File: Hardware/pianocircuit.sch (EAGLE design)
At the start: 180 parts

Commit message: Updated Schematic
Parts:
- removed C10, C13, C14, C16, C17, C18, C19, C20, C26, C27, C28, C29, C30, C38, C39, C40, C41, C42, C50, C51, C52, C53, C54, C8, C9: (no value), LinnesLab-Passives:CAPACITOR0603
- removed C15, C25, C37, C49, C7: 100n, LinnesLab-Passives:CAPACITOR0603
- removed OP13, OP14, OP17, OP18, OP3, OP4, OP5, OP7, OP8, OP9: (no value), LinnesLab-AnalogIC:OP-DUALR
- removed R10, R19, R33, R42, R55, R73: 3.3M, LinnesLab-Passives:RESISTOR0603
- removed R11, R12, R13, R14, R20, R21, R22, R23, R34, R35, R36, R37, R56, R57, R58, R59, R74, R75, R76, R77: 10k, LinnesLab-Passives:RESISTOR0603
- removed R15, R16, R17, R18, R24, R25, R31, R32, R38, R39, R40, R41, R60, R61, R62, R63, R78, R79, R80, R81: (no value), LinnesLab-Passives:RESISTOR0603
- removed SW3, SW4, SW5, SW7, SW9: (no value), LinnesLab-Switches:SPST.KT11P4SM34LFS
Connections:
- removed net N$100: SW9.B
- removed net N$13: OP3A.+IN, R13.1, R14.2
- removed net N$14: C7.2, OP3A.-IN, OP3A.OUT, R12.1
- removed net N$15: OP3B.-IN, R11.1, R12.2
- removed net N$16: C7.1, OP3B.+IN, R10.1
- removed net N$17: OP3B.OUT, R10.2, R11.2, R15.1
- removed net N$18: C9.1, R15.2, R16.1
- removed net N$19: C10.1, R16.2, R17.1
- removed net N$20: C13.1, R17.2, R18.1
- removed net N$21: C14.1, OP4A.+IN, R18.2
- removed net N$22: OP4A.-IN, OP4A.OUT, SW3.A
- removed net N$23: SW3.B
- removed net N$24: OP5A.+IN, R22.1, R23.2
- removed net N$25: C15.2, OP5A.-IN, OP5A.OUT, R21.1
- removed net N$26: OP5B.-IN, R20.1, R21.2
- removed net N$32: C15.1, OP5B.+IN, R19.1
- removed net N$33: OP5B.OUT, R19.2, R20.2, R24.1
- removed net N$34: C17.1, R24.2, R25.1
- removed net N$35: C18.1, R25.2, R31.1
- removed net N$36: C19.1, R31.2, R32.1
- removed net N$37: C20.1, OP7A.+IN, R32.2
- removed net N$38: OP7A.-IN, OP7A.OUT, SW4.A
- removed net N$39: SW4.B
- removed net N$40: OP8A.+IN, R36.1, R37.2
- removed net N$41: C25.2, OP8A.-IN, OP8A.OUT, R35.1
- removed net N$42: OP8B.-IN, R34.1, R35.2
- removed net N$43: C25.1, OP8B.+IN, R33.1
- removed net N$44: OP8B.OUT, R33.2, R34.2, R38.1
- removed net N$45: C27.1, R38.2, R39.1
- removed net N$46: C28.1, R39.2, R40.1
- removed net N$47: C29.1, R40.2, R41.1
- removed net N$48: C30.1, OP9A.+IN, R41.2
- removed net N$49: OP9A.-IN, OP9A.OUT, SW5.A
- removed net N$50: SW5.B
- removed net N$68: OP13A.+IN, R58.1, R59.2
- removed net N$69: C37.2, OP13A.-IN, OP13A.OUT, R57.1
- removed net N$70: OP13B.-IN, R56.1, R57.2
- removed net N$71: C37.1, OP13B.+IN, R55.1
- removed net N$72: OP13B.OUT, R55.2, R56.2, R60.1
- removed net N$73: C39.1, R60.2, R61.1
- removed net N$74: C40.1, R61.2, R62.1
- removed net N$75: C41.1, R62.2, R63.1
- removed net N$76: C42.1, OP14A.+IN, R63.2
- removed net N$77: OP14A.-IN, OP14A.OUT, SW7.A
- removed net N$78: SW7.B
- removed net N$90: OP17A.+IN, R76.1, R77.2
- removed net N$91: C49.2, OP17A.-IN, OP17A.OUT, R75.1
- removed net N$92: OP17B.-IN, R74.1, R75.2
- removed net N$93: C49.1, OP17B.+IN, R73.1
- removed net N$94: OP17B.OUT, R73.2, R74.2, R78.1
- removed net N$95: C51.1, R78.2, R79.1
- removed net N$96: C52.1, R79.2, R80.1
- removed net N$97: C53.1, R80.2, R81.1
- removed net N$98: C54.1, OP18A.+IN, R81.2
- removed net N$99: OP18A.-IN, OP18A.OUT, SW9.A
- net GND: no longer C10.2, C13.2, C14.2, C17.2, C18.2, C19.2, C20.2, C27.2, C28.2, C29.2, C30.2, C39.2, C40.2, C41.2, C42.2, C51.2, C52.2, C53.2, C54.2, C9.2, OP13P.V-, OP17P.V-, OP3P.V-, OP5P.V-, OP8P.V-, R14.1, R23.1, R37.1, R59.1, R77.1
- net N$2: no longer C16.1, C26.1, C38.1, C50.1, C8.1
- net N$60: no longer R42.1
- net N$61: no longer R42.2
- net V_BATT: no longer C16.2, C26.2, C38.2, C50.2, C8.2, OP13P.V+, OP17P.V+, OP3P.V+, OP5P.V+, OP8P.V+, R13.2, R22.2, R36.2, R58.2, R76.2
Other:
- moved on the sheet: C43, C44, C45, C46, C47, C48, OP15B, OP15P, OP16A, R64, R65, R66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

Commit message: Full Schematic
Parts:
- removed C43, C55: 100n, LinnesLab-Passives:CAPACITOR0603
- removed C44, C45, C46, C47, C48, C56, C57, C58, C59, C60: (no value), LinnesLab-Passives:CAPACITOR0603
- removed OP15, OP16, OP19, OP20: (no value), LinnesLab-AnalogIC:OP-DUALR
- removed R64, R82: 3.3M, LinnesLab-Passives:RESISTOR0603
- removed R65, R66, R67, R68, R83, R84, R85, R86: 10k, LinnesLab-Passives:RESISTOR0603
- removed R69, R70, R71, R72, R87, R88, R89, R90: (no value), LinnesLab-Passives:RESISTOR0603
- removed SW10, SW8: (no value), LinnesLab-Switches:SPST.KT11P4SM34LFS
- added C10: 330p, LinnesLab-Passives:CAPACITOR0603
- added C13: 50n, LinnesLab-Passives:CAPACITOR0603
- added C14: 250u, LinnesLab-Passives:CAPACITOR.POLARC-EEU-FM-A-220UF
- added C7, C8, C9: 33n, LinnesLab-Passives:CAPACITOR0603
- added IC1: LM386M-1, linear:LM386M-1
- added OP3: (no value), LinnesLab-AnalogIC:OP-DUALR
- added R10, R11, R12: 39k, LinnesLab-Passives:RESISTOR0603
- added R13, R14, R16: 10k, LinnesLab-Passives:RESISTOR0603
- added R15: 390k, LinnesLab-Passives:RESISTOR0603
- added R17: (no value), LinnesLab-Passives:R-TRIMM-CB10V
- added SPK1: (no value), LinnesLab-Electromechanical:SPEAKER
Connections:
- removed net N$101: OP19A.+IN, R85.1, R86.2
- removed net N$102: C55.2, OP19A.-IN, OP19A.OUT, R84.1
- removed net N$103: OP19B.-IN, R83.1, R84.2
- removed net N$104: C55.1, OP19B.+IN, R82.1
- removed net N$105: OP19B.OUT, R82.2, R83.2, R87.1
- removed net N$106: C57.1, R87.2, R88.1
- removed net N$107: C58.1, R88.2, R89.1
- removed net N$108: C59.1, R89.2, R90.1
- removed net N$109: C60.1, OP20A.+IN, R90.2
- removed net N$110: OP20A.-IN, OP20A.OUT, SW10.A
- removed net N$111: SW10.B
- removed net N$12: SW2.B
- removed net N$59: SW1.B
- removed net N$67: SW6.B
- removed net N$79: OP15A.+IN, R67.1, R68.2
- removed net N$80: C43.2, OP15A.-IN, OP15A.OUT, R66.1
- removed net N$81: OP15B.-IN, R65.1, R66.2
- removed net N$82: C43.1, OP15B.+IN, R64.1
- removed net N$83: OP15B.OUT, R64.2, R65.2, R69.1
- removed net N$84: C45.1, R69.2, R70.1
- removed net N$85: C46.1, R70.2, R71.1
- removed net N$86: C47.1, R71.2, R72.1
- removed net N$87: C48.1, OP16A.+IN, R72.2
- removed net N$88: OP16A.-IN, OP16A.OUT, SW8.A
- removed net N$89: SW8.B
- new net A3: R12.2, SW6.B
- new net C3: R10.2, SW2.B
- new net F3: R11.2, SW1.B
- new net N$14: C7.2, R10.1
- new net N$15: C10.2, C7.1, C8.1, C9.1, OP3A.+IN, R15.2
- new net N$16: C9.2, R12.1
- new net N$17: C8.2, R11.1
- new net N$20: C10.1, OP3A.OUT, R15.1, R17.E
- new net N$21: OP3A.-IN, R13.1, R14.1
- new net N$22: IC1.-IN, R17.S
- new net N$23: C13.2, R16.2
- new net N$26: C13.1, C14.+, IC1.OUT
- new net N$32: C14.-, SPK1.+
- net GND: now also IC1.+IN, IC1.GND, R14.2, R16.1, SPK1.-; no longer C45.2, C46.2, C47.2, C48.2, C57.2, C58.2, C59.2, C60.2, OP15P.V-, OP19P.V-, R68.1, R86.1
- net N$2: no longer C44.1, C56.1
- net V_BATT: now also IC1.VS, R13.2; no longer C44.2, C56.2, OP15P.V+, OP19P.V+, R67.2, R85.2

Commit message: Updated Schematic
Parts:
- removed C2, C32: (no value), LinnesLab-Passives:CAPACITOR0603
- removed R4, R45, R46, R5: 10k, LinnesLab-Passives:RESISTOR0603
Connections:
- removed net N$1: OP1A.+IN, R4.1, R5.2
- removed net N$28: C11.2, OP6A.-IN, OP6A.OUT, R28.1
- removed net N$51: OP10A.+IN, R45.1, R46.2
- removed net N$56: C31.2, OP10A.-IN, OP10A.OUT, R44.1
- net GND: no longer OP10P.V-, OP1P.V-, R46.1, R5.1
- net N$2: no longer C2.1, C32.1
- net N$3: now also C11.2, C31.2, OP6A.-IN, OP6A.OUT, R28.1, R44.1; no longer OP1A.-IN, OP1A.OUT
- net V_BATT: no longer C2.2, C32.2, OP10P.V+, OP1P.V+, R4.2, R45.2

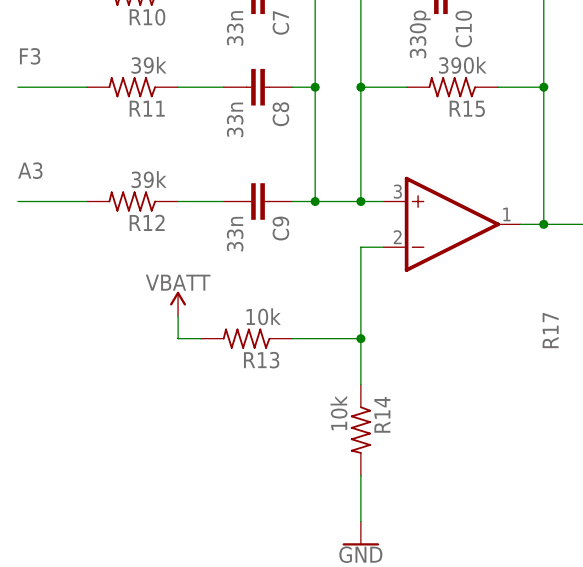
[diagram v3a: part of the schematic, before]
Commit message: Routed Board and Updated Schematic
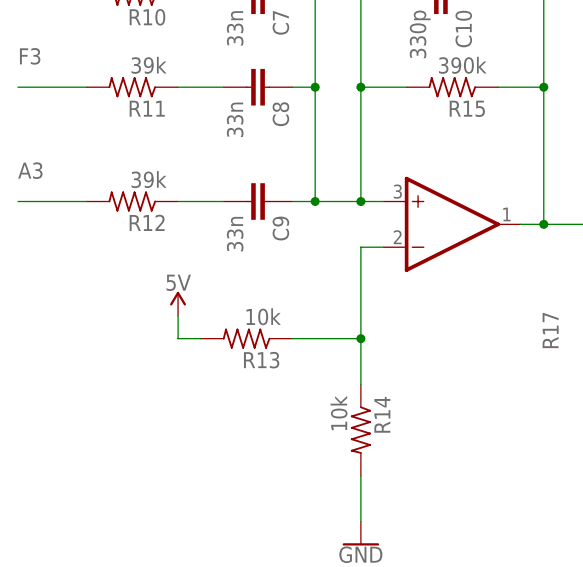
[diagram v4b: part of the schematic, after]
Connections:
- net V_BATT renamed 5V
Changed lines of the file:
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@@
 <part name="C13" library="LinnesLab-Passives" deviceset="CAPACITOR" device="0603" package3d_urn="urn:adsk.eagle:package:15661989/2" value="50n"/>
 <part name="GND8" library="LinnesLab-Symbols" deviceset="GND" device=""/>
-<part name="SUPPLY3" library="LinnesLab-Symbols" deviceset="VBATT" device=""/>
+<part name="SUPPLY3" library="LinnesLab-Symbols" deviceset="VBATT" device="" value="5V"/>
 <part name="OP3" library="LinnesLab-AnalogIC" deviceset="OP-DUAL" device="R" package3d_urn="urn:adsk.eagle:package:15818288/2"/>
 <part name="SPK1" library="LinnesLab-Electromechanical" deviceset="SPEAKER" device=""/>
@@
 </segment>
 </net>
-<net name="V_BATT" class="0">
+<net name="5V" class="0">
 <segment>
 <pinref part="R29" gate="G$1" pin="2"/>

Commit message: board and schematic
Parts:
- added R4: 3.3M, LinnesLab-Passives:RESISTOR0603
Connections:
- new net N$12: R4.2
- net N$60: now also R4.1
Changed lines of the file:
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@@
 <part name="SUPPLY4" library="LinnesLab-Symbols" deviceset="VBATT" device="" value="5V"/>
 <part name="GND12" library="LinnesLab-Symbols" deviceset="GND" device=""/>
+<part name="R4" library="LinnesLab-Passives" deviceset="RESISTOR" device="0603" package3d_urn="urn:adsk.eagle:package:15661944/2" value="3.3M"/>
 </parts>
 <sheets>
@@
 <instance part="GND12" gate="G$1" x="91.44" y="-55.88" smashed="yes">
 <attribute name="VALUE" x="91.44" y="-56.134" size="1.778" layer="96" align="top-center"/>
+</instance>
+<instance part="R4" gate="G$1" x="553.72" y="93.98" smashed="yes">
+<attribute name="VALUE" x="549.91" y="90.678" size="1.778" layer="96"/>
 </instance>
 </instances>
@@
 <pinref part="C31" gate="G$1" pin="1"/>
 <pinref part="OP10" gate="B" pin="+IN"/>
-<wire x1="535.94" y1="81.28" x2="551.18" y2="81.28" width="0.1524" layer="91"/>
+<wire x1="535.94" y1="81.28" x2="546.1" y2="81.28" width="0.1524" layer="91"/>
+<wire x1="546.1" y1="81.28" x2="551.18" y2="81.28" width="0.1524" layer="91"/>
+<wire x1="546.1" y1="81.28" x2="546.1" y2="93.98" width="0.1524" layer="91"/>
+<pinref part="R4" gate="G$1" pin="1"/>
+<wire x1="546.1" y1="93.98" x2="548.64" y2="93.98" width="0.1524" layer="91"/>
+<junction x="546.1" y="81.28"/>
 </segment>
 </net>
@@
 </segment>
 </net>
+<net name="N$12" class="0">
+<segment>
+<pinref part="R4" gate="G$1" pin="2"/>
+<wire x1="558.8" y1="93.98" x2="571.5" y2="93.98" width="0.1524" layer="91"/>
+<wire x1="571.5" y1="93.98" x2="571.5" y2="78.74" width="0.1524" layer="91"/>
+</segment>
+</net>

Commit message: Fixed inconsistent board and schematic
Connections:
- net 5V renamed V+
- net GND renamed V-
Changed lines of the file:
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@@
 </busses>
 <nets>
-<net name="GND" class="0">
+<net name="V-" class="0">
 <segment>
 <pinref part="GND16" gate="G$1" pin="GND"/>
@@
 </segment>
 </net>
-<net name="5V" class="0">
+<net name="V+" class="0">
 <segment>
 <pinref part="R29" gate="G$1" pin="2"/>
@@
 </sheet>
 </sheets>
+<errors>
+</errors>
 </schematic>
 </drawing>
